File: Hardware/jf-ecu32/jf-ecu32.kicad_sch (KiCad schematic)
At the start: 31 parts, among them J1 GAZ, J10 k, J11 RPM, J12 S.PORT, J2 AUX, J3 PPM/PWM, J4 STARTER, J5 GLOW, J6 VANNE KEROSTART, J7 VANNE KERO, J8 BATTERY 2S/3S, J9 STARTER, Q1 QM6006D, Q2 QM6006D, Q3 QM6006D, Q4 QM6006D, U1 ESP32-DevKitC, U2 4050, U3 MAX31855KASA, U4 AMS1117-3.3, U5 4050

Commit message: update
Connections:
- net RX2 is gone; now on net PWM_KEROSTART_3.3: U1.27 (GPIO16)
- net AUX: now also U1.36 (GPIO22); no longer U1.6 (VDET_2/GPIO35/ADC1_CH7)
- net PPM_GAZ: now also U1.10 (DAC_2/ADC2_CH9/GPIO26); no longer U1.5 (VDET_1/GPIO34/ADC1_CH6)
- net PPM_PWM_PUMP1_3.3: now also U1.5 (VDET_1/GPIO34/ADC1_CH6); no longer U1.21 (SD_DATA0/GPIO7)
- net PPM_PWM_PUMP2_3.3: now also U1.6 (VDET_2/GPIO35/ADC1_CH7); no longer U1.20 (SD_CLK/GPIO6)
- net PPM_STARTER_3.3: now also U1.8 (32K_XN/GPIO33/ADC1_CH5); no longer U1.25 (*GPIO0/BOOT/ADC2_CH1)
- net PWM_GLOW_3.3: now also U1.7 (32K_XP/GPIO32/ADC1_CH4); no longer U1.24 (ADC2_CH2/*GPIO2)
- net PWM_KEROSTART_3.3: no longer U1.23 (*MTDO/GPIO15/ADC2_CH3)
- net PWM_KERO_3.3: now also U1.25 (*GPIO0/BOOT/ADC2_CH1); no longer U1.22 (SD_DATA1/GPIO8)
- net RPM: now also U1.33 (GPIO21); no longer U1.7 (32K_XP/GPIO32/ADC1_CH4)

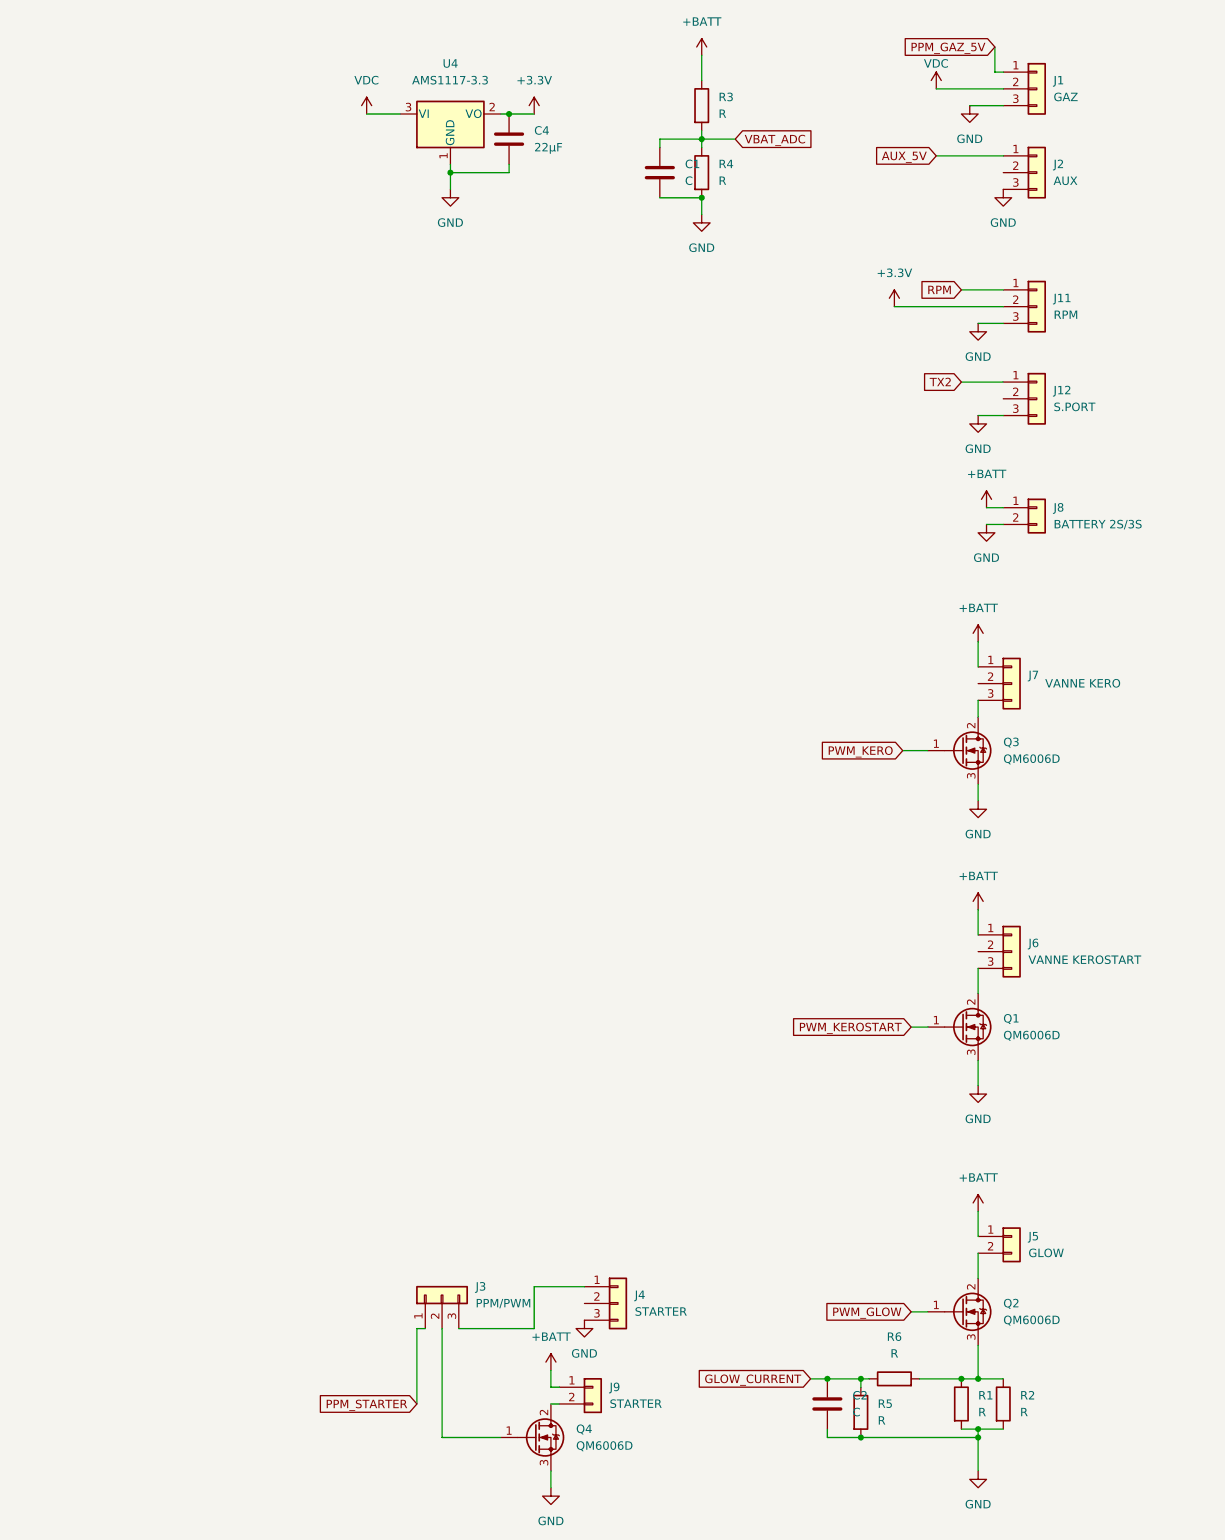
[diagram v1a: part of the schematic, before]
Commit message: Ajout des nouveautés
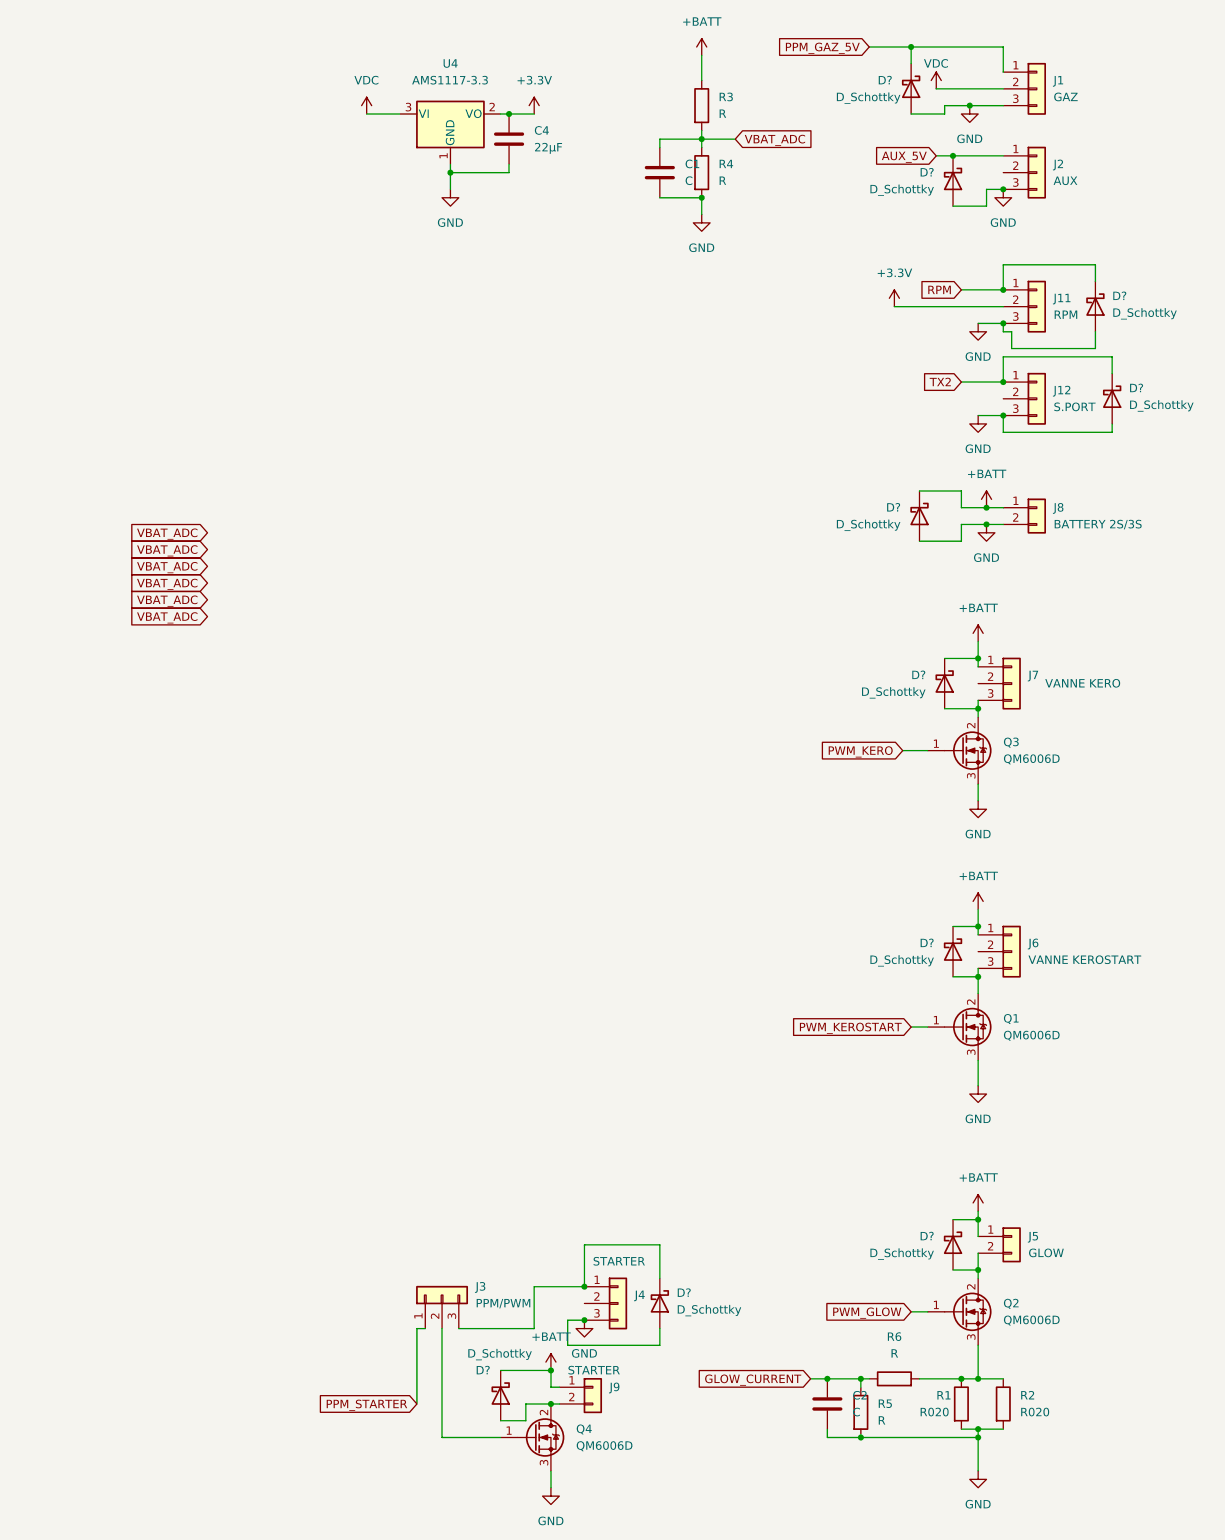
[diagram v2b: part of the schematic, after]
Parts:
- added D? (x10): D_Schottky, symbol Device:D_Schottky
- R1, R2: value R -> R020
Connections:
- net +BATT: now also D?.1 (K), D?.1 (K), D?.1 (K), D?.1 (K), D?.1 (K)
- net AUX_5V: now also D?.1 (K)
- net GND: now also D?.2 (A), D?.2 (A), D?.2 (A), D?.2 (A), D?.2 (A), D?.2 (A)
- net PPM_GAZ_5V: now also D?.1 (K)
- net RPM: now also D?.1 (K)
- net TX2: now also D?.1 (K)
- net at J9.2 (Pin_2), Q4.2 (D): now also D?.2 (A)
- net at J5.2 (Pin_2), Q2.2 (D): now also D?.2 (A)
- net at J6.3 (Pin_3), Q1.2 (D): now also D?.2 (A)
- net at J7.3 (Pin_3), Q3.2 (D): now also D?.2 (A)
- net at J3.3 (Pin_3), J4.1 (Pin_1): now also D?.1 (K)

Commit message: update
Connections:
- net PPM_PWM_PUMP1_3.3: now also U1.9 (DAC_1/ADC2_CH8/GPIO25); no longer U1.5 (VDET_1/GPIO34/ADC1_CH6)
- net PPM_PWM_PUMP2_3.3: no longer U1.6 (VDET_2/GPIO35/ADC1_CH7)
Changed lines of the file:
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@@
-    (stroke (width 0) (type default) (color 0 0 0 0))
-  )
-  (wire (pts (xy 116.84 53.34) (xy 120.65 53.34))
     (stroke (width 0) (type default) (color 0 0 0 0))
   )
@@
     (stroke (width 0) (type default) (color 0 0 0 0))
   )
+  (wire (pts (xy 116.84 60.96) (xy 120.65 60.96))
+    (stroke (width 0) (type default) (color 0 0 0 0))
+  )
   (wire (pts (xy 382.27 222.25) (xy 384.81 222.25))
     (stroke (width 0) (type default) (color 0 0 0 0))
@@
     (stroke (width 0) (type default) (color 0 0 0 0))
   )
-  (wire (pts (xy 116.84 50.8) (xy 120.65 50.8))
-    (stroke (width 0) (type default) (color 0 0 0 0))
-  )
   (wire (pts (xy 382.27 57.15) (xy 388.62 57.15))
     (stroke (width 0) (type default) (color 0 0 0 0))
@@
     )
   )
-  (global_label "PPM_PWM_PUMP1_3.3" (shape input) (at 116.84 50.8 180) (fields_autoplaced)
-    (effects (font (size 1.27 1.27)) (justify right))
-    (property "Intersheet References" "${INTERSHEET_REFS}" (id 0) (at 93.8045 50.7206 0)
+  (global_label "PPM_PWM_PUMP1_3.3" (shape input) (at 116.84 60.96 180) (fields_autoplaced)
+    (effects (font (size 1.27 1.27)) (justify right))
+    (property "Intersheet References" "${INTERSHEET_REFS}" (id 0) (at 93.8045 60.8806 0)
       (effects (font (size 1.27 1.27)) (justify right) hide)
     )
@@
     )
   )
-  (global_label "PPM_PWM_PUMP2_3.3" (shape input) (at 116.84 53.34 180) (fields_autoplaced)
-    (effects (font (size 1.27 1.27)) (justify right))
-    (property "Intersheet References" "${INTERSHEET_REFS}" (id 0) (at 93.8045 53.2606 0)
-      (effects (font (size 1.27 1.27)) (justify right) hide)
-    )
+  (global_label "PPM_PWM_PUMP2_3.3" (shape input) (at 101.6 22.86 180) (fields_autoplaced)
+    (effects (font (size 1.27 1.27)) (justify right))
+    (property "Intersheet References" "${INTERSHEET_REFS}" (id 0) (at 78.5645 22.7806 0)
+      (effects (font (size 1.27 1.27)) (justify right) hide)
+    )

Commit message: PCB update
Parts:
- added BT1: Battery_Cell, Battery:Battery_Panasonic_CR2032-VS1N_Vertical_CircularHoles, symbol Device:Battery_Cell
- added D1, D13, D14, D15, D16, D2: D_Schottky, Diode_SMD:D_SMC, symbol Device:D_Schottky
- added J13, J16: PPM/PWM, Connector_PinHeader_2.54mm:PinHeader_1x03_P2.54mm_Vertical, symbol Connector_Generic:Conn_01x03
- added J14: PUMP1, Connector_AMASS:AMASS_XT30U-F_1x02_P5.0mm_Vertical, symbol Connector_Generic:Conn_01x02
- added J15: PUMP1, Connector_PinHeader_2.54mm:PinHeader_1x03_P2.54mm_Vertical, symbol Connector_Generic:Conn_01x03
- added J17: PUMP2, Connector_AMASS:AMASS_XT30U-F_1x02_P5.0mm_Vertical, symbol Connector_Generic:Conn_01x02
- added J18: PUMP2, Connector_PinHeader_2.54mm:PinHeader_1x03_P2.54mm_Vertical, symbol Connector_Generic:Conn_01x03
- added Q5, Q6: QM6006D, Package_TO_SOT_SMD:TO-252-2, symbol Transistor_FET:QM6006D
- added R10, R11, R12, R7, R8, R9: R, Resistor_SMD:R_0603_1608Metric, symbol Device:R
- D10, D11, D12, D3, D4, D5, D6, D7, D8, D9: renamed from D?; footprint (none) -> Diode_SMD:D_SMC
- U1: footprint Espressif:ESP32-DevKitC -> RF_Module:ESP32-WROOM-32
- U5: footprint (none) -> Package_SO:SOP-16_3.9x9.9mm_P1.27mm
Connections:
- net +3.3V: now also D1.2 (A); no longer U1.1 (3V3)
- net +BATT: now also J5.2 (Pin_2), J8.2 (Pin_2), J9.2 (Pin_2), D13.1 (K), D15.1 (K), J14.2 (Pin_2), J17.2 (Pin_2); no longer J5.1 (Pin_1), J8.1 (Pin_1), J9.1 (Pin_1)
- net GND: now also J8.1 (Pin_1), BT1.2 (-), D14.2 (A), D16.2 (A), J15.3 (Pin_3), J18.3 (Pin_3), Q5.3 (S), Q6.3 (S), R10.2, R11.2, R12.2, R7.2, R8.2, R9.2; no longer J8.2 (Pin_2)
- net PPM_PWM_PUMP1: now also J13.2 (Pin_2)
- net PPM_PWM_PUMP1_3.3: now also U1.5 (VDET_1/GPIO34/ADC1_CH6); no longer U1.9 (DAC_1/ADC2_CH8/GPIO25)
- net PPM_PWM_PUMP2: now also J16.2 (Pin_2)
- net PPM_PWM_PUMP2_3.3: now also U1.6 (VDET_2/GPIO35/ADC1_CH7)
- net PPM_STARTER_3.3: now also U5.9; no longer U5.3
- net PWM_GLOW: now also R11.1
- net PWM_KERO: now also U5.2, R12.1; no longer U5.10
- net PWM_KEROSTART: now also R10.1
- net PWM_KERO_3.3: now also U5.3; no longer U5.9
- net VBAT_ADC: now also U1.1 (3V3), D1.1 (K), D2.1 (K)
- net at D3.2 (A), Q4.2 (D): now also J9.1 (Pin_1); no longer J9.2 (Pin_2)
- net at Q4.1 (G): now also J3.1 (Pin_1), R9.1; no longer J3.2 (Pin_2)
- net at D10.2 (A), Q2.2 (D): now also J5.1 (Pin_1); no longer J5.2 (Pin_2)
- removed net PPM_STARTER: J3.1 (Pin_1), U5.2
- new net: D14.1 (K), J13.3 (Pin_3), J15.1 (Pin_1)
- new net: D16.1 (K), J16.3 (Pin_3), J18.1 (Pin_1)
- new net: J13.1 (Pin_1), Q5.1 (G), R7.1
- new net: D13.2 (A), J14.1 (Pin_1), Q5.2 (D)
- new net: BT1.1 (+), D2.2 (A)
- new net: D15.2 (A), J17.1 (Pin_1), Q6.2 (D)
- new net: J16.1 (Pin_1), Q6.1 (G), R8.1
- new net PPM_PWM_STARTER: J3.2 (Pin_2), U5.10
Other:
- moved on the sheet: J8

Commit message: PCB
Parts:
- C1, C2: footprint (none) -> Capacitor_SMD:C_0603_1608Metric
- C3, C4: footprint (none) -> Capacitor_SMD:CP_Elec_5x3
- D1, D10, D11, D12, D13, D14, D15, D16, D2, D3, D4, D5, D6, D7, D8, D9: footprint Diode_SMD:D_SMC -> Diode_SMD:D_SMB
- U2, U5: footprint Package_SO:SOP-16_3.9x9.9mm_P1.27mm -> Package_SO:SOP-16_4.4x10.4mm_P1.27mm

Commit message: pcb
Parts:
- removed Q1, Q3: QM6006D, Package_TO_SOT_SMD:TO-252-2, symbol Transistor_FET:QM6006D
- added D17: BZV55C3V3, Diode_SMD:D_MiniMELF, symbol Diode:BZV55C3V3
- added Q1, Q3: AO3400A, Package_TO_SOT_SMD:SOT-23, symbol Transistor_FET:AO3400A
- D1, D10, D11, D12, D13, D14, D15, D16, D2, D3, D4, D5, D6, D7, D8, D9: footprint Diode_SMD:D_SMB -> Diode_SMD:D_SMA
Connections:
- net +3.3V: now also D17.1 (K)
- net +BATT: now also J6.2 (Pin_2), J7.2 (Pin_2); no longer J6.1 (Pin_1), J7.1 (Pin_1)
- net GND: now also D17.2 (A), Q1.2 (S), Q3.2 (S)
- net PPM_PWM_PUMP2: now also U5.10; no longer U5.15
- net PPM_PWM_PUMP2_3.3: now also U5.9; no longer U5.14
- net PPM_PWM_STARTER: now also U5.15; no longer U5.10
- net PPM_STARTER_3.3: now also U5.14; no longer U5.9
- net PWM_KERO: now also Q1.1 (G)
- net PWM_KEROSTART: now also Q3.1 (G)
- net at D9.2 (A), J6.3 (Pin_3): now also J6.1 (Pin_1), Q3.3 (D)
- net at D7.2 (A), J7.3 (Pin_3): now also J7.1 (Pin_1), Q1.3 (D)
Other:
- moved on the sheet: D7, D9

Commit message: PCB
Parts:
- BT1: footprint Battery:Battery_Panasonic_CR2032-VS1N_Vertical_CircularHoles -> Battery:BatteryHolder_Keystone_1058_1x2032
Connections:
- net VBAT_ADC: no longer D1.1 (K), D2.1 (K), U1.1 (3V3)
- new net V_CPU: D1.1 (K), D2.1 (K), U1.1 (3V3)
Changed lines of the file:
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@@
   (junction (at 375.92 168.91) (diameter 0) (color 0 0 0 0)
   )
-  (junction (at 120.65 35.56) (diameter 0) (color 0 0 0 0)
-  )
   (junction (at 388.62 41.91) (diameter 0) (color 0 0 0 0)
   )
@@
     (stroke (width 0) (type default) (color 0 0 0 0))
   )
-  (wire (pts (xy 120.65 35.56) (xy 120.65 40.64))
-    (stroke (width 0) (type default) (color 0 0 0 0))
-  )
   (wire (pts (xy 388.62 78.74) (xy 405.13 78.74))
     (stroke (width 0) (type default) (color 0 0 0 0))
@@
     (stroke (width 0) (type default) (color 0 0 0 0))
   )
-  (wire (pts (xy 120.65 31.75) (xy 120.65 35.56))
+  (wire (pts (xy 120.65 31.75) (xy 118.11 40.64))
     (stroke (width 0) (type default) (color 0 0 0 0))
   )
@@
     (stroke (width 0) (type default) (color 0 0 0 0))
   )
+  (wire (pts (xy 118.11 40.64) (xy 120.65 40.64))
+    (stroke (width 0) (type default) (color 0 0 0 0))
+  )
   (wire (pts (xy 313.69 39.37) (xy 326.39 39.37))
     (stroke (width 0) (type default) (color 0 0 0 0))
@@
     (stroke (width 0) (type default) (color 0 0 0 0))
   )
-  (wire (pts (xy 116.84 35.56) (xy 120.65 35.56))
-    (stroke (width 0) (type default) (color 0 0 0 0))
-  )
   (wire (pts (xy 116.84 45.72) (xy 120.65 45.72))
     (stroke (width 0) (type default) (color 0 0 0 0))
@@
     )
   )
-  (global_label "VBAT_ADC" (shape input) (at 259.08 20.32 180) (fields_autoplaced)
-    (effects (font (size 1.27 1.27)) (justify right))
-    (property "Intersheet References" "${INTERSHEET_REFS}" (id 0) (at 247.6559 20.2406 0)
-      (effects (font (size 1.27 1.27)) (justify right) hide)
-    )
-  )
   (global_label "GLOW_CURRENT" (shape input) (at 116.84 48.26 180) (fields_autoplaced)
     (effects (font (size 1.27 1.27)) (justify right))
@@
     )
   )
+  (global_label "V_CPU" (shape input) (at 118.11 40.64 180) (fields_autoplaced)
+    (effects (font (size 1.27 1.27)) (justify right))
+    (property "Intersheet References" "${INTERSHEET_REFS}" (id 0) (at 109.7702 40.5606 0)
+      (effects (font (size 1.27 1.27)) (justify right) hide)
+    )
+  )
   (global_label "PWM_KEROSTART_3.3" (shape input) (at 73.66 146.05 0) (fields_autoplaced)
     (effects (font (size 1.27 1.27)) (justify left))
@@
     )
   )
-  (global_label "VBAT_ADC" (shape input) (at 116.84 35.56 180) (fields_autoplaced)
-    (effects (font (size 1.27 1.27)) (justify right))
-    (property "Intersheet References" "${INTERSHEET_REFS}" (id 0) (at 105.4159 35.4806 0)
-      (effects (font (size 1.27 1.27)) (justify right) hide)
-    )
-  )
   (global_label "PWM_KERO" (shape input) (at 373.38 127 180) (fields_autoplaced)
     (effects (font (size 1.27 1.27)) (justify right))
@@
     )
   )
+  (global_label "V_CPU" (shape input) (at 259.08 20.32 180) (fields_autoplaced)
+    (effects (font (size 1.27 1.27)) (justify right))
+    (property "Intersheet References" "${INTERSHEET_REFS}" (id 0) (at 250.7402 20.2406 0)
+      (effects (font (size 1.27 1.27)) (justify right) hide)
+    )
+  )
   (global_label "PPM_GAZ" (shape input) (at 66.04 43.18 0) (fields_autoplaced)
     (effects (font (size 1.27 1.27)) (justify left))
@@
       (effects (font (size 1.27 1.27)) (justify left))
     )
-    (property "Footprint" "Battery:Battery_Panasonic_CR2032-VS1N_Vertical_CircularHoles" (id 2) (at 259.08 39.116 90)
+    (property "Footprint" "Battery:BatteryHolder_Keystone_1058_1x2032" (id 2) (at 259.08 39.116 90)
       (effects (font (size 1.27 1.27)) hide)
     )
@@
     )
     (path "/55c603d0-b317-4faf-b668-b40872cb1ab4"
-      (reference "BT1") (unit 1) (value "Battery_Cell") (footprint "Battery:Battery_Panasonic_CR2032-VS1N_Vertical_CircularHoles")
+      (reference "BT1") (unit 1) (value "Battery_Cell") (footprint "Battery:BatteryHolder_Keystone_1058_1x2032")
     )
     (path "/842255f1-0ffe-4d64-bdf3-df180013631d"
